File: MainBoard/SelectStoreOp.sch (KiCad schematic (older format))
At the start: 18 parts, among them U32 74ABT245, U33 74ABT245, U34 74AHCT138, U35 74ABT245, U36 74ABT245, U37 74ABT245, U38 74ABT245, U39 74ABT245, U40 74ABT245

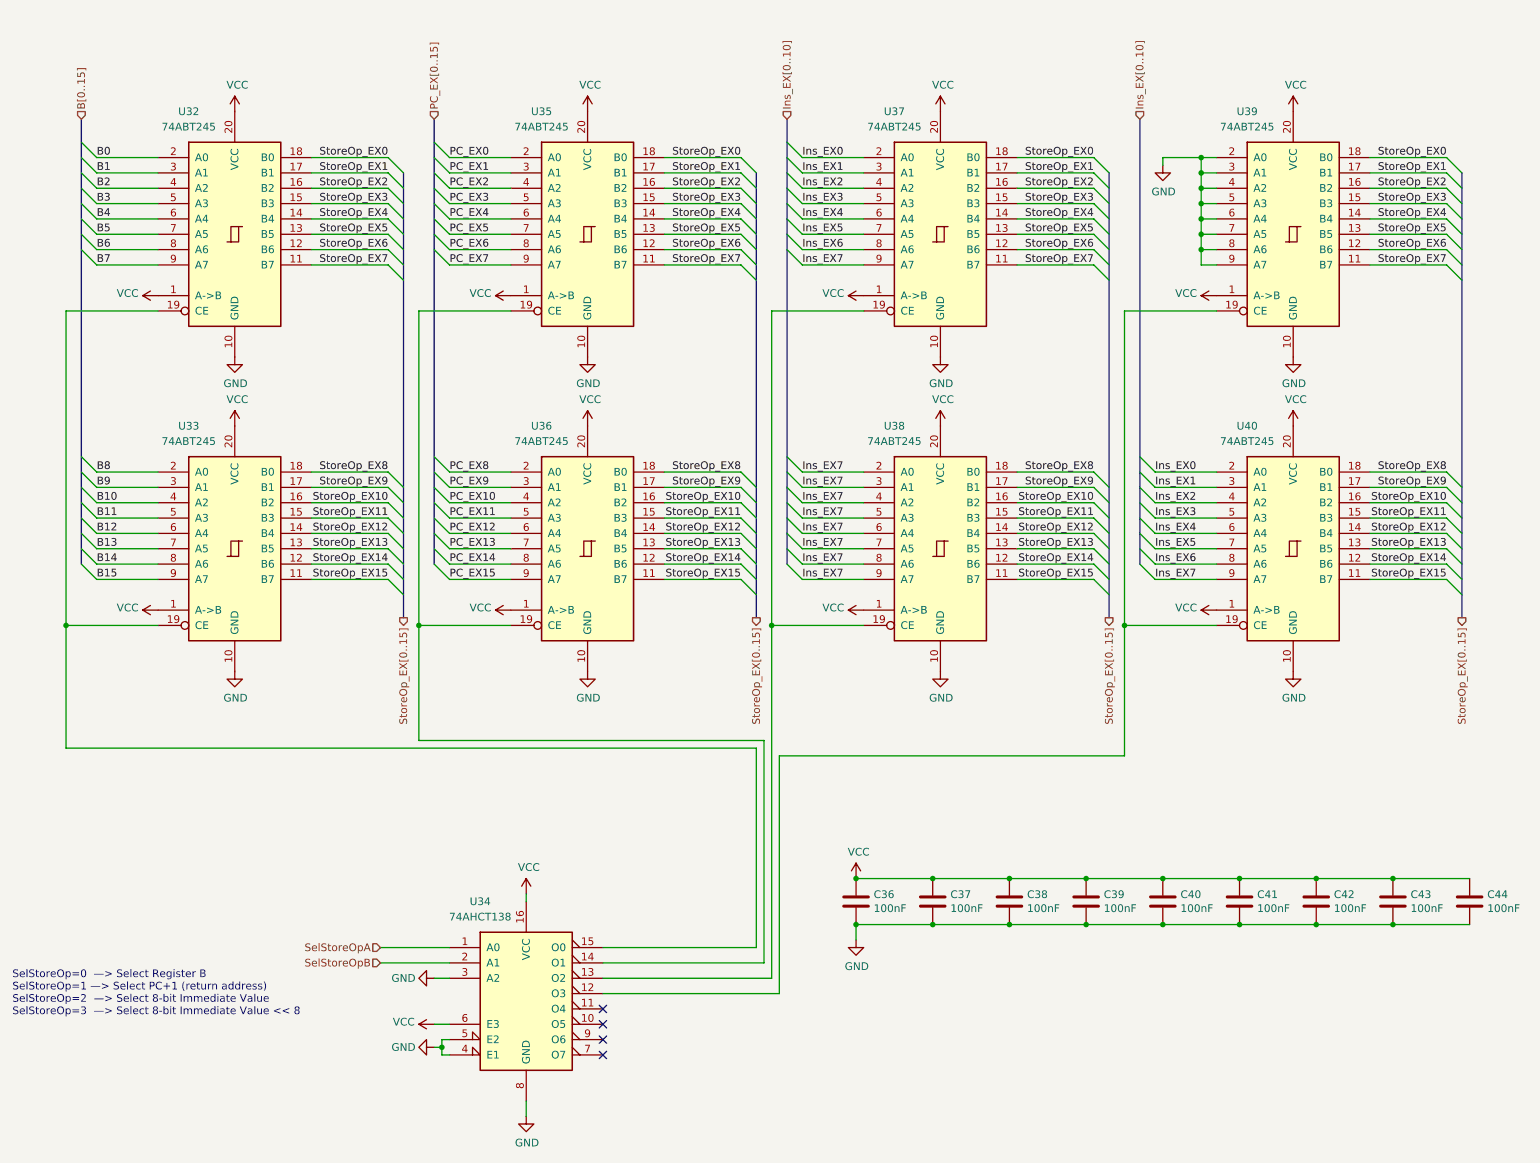
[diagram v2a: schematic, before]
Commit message: Replace 74AHCT245 with 74AHCT16245. Ditto 74ABT25.
This greatly reduces the number of components and saves a lot of board
space. (Note that PCB layout has been undone in areas related to changes.)
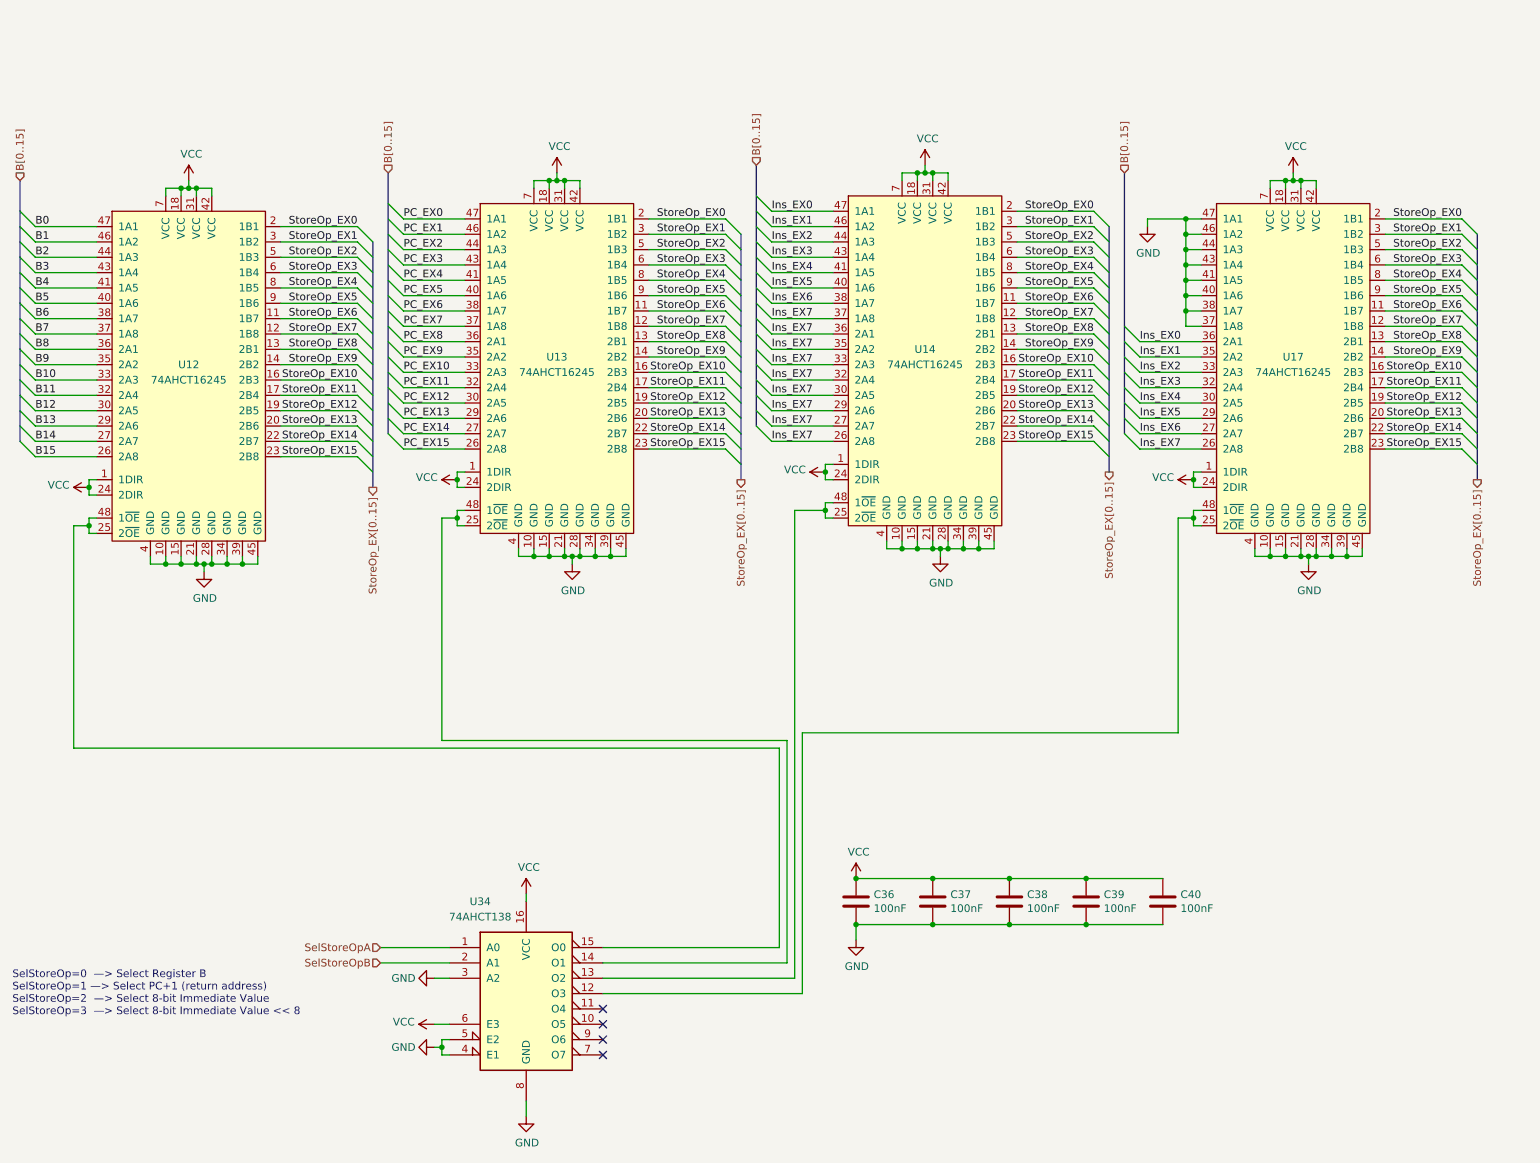
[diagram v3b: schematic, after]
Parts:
- removed C41, C42, C43, C44: 100nF, Capacitor_SMD:C_0603_1608Metric_Pad1.08x0.95mm_HandSolder, symbol Device:C
- removed U32, U33, U35, U36, U37, U38, U39, U40: 74ABT245, Package_SO:TSSOP-20_4.4x6.5mm_P0.65mm, symbol MainBoard-rescue:74LS245-74xx
- added U12, U13, U14, U17: 74AHCT16245, Package_SO:TSSOP-48_6.1x12.5mm_P0.5mm, symbol 74xx:74AHCT16245
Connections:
- net B0: now also U12.47 (1A1)
- net B1: now also U12.46 (1A2)
- net B10: now also U12.33 (2A3)
- net B11: now also U12.32 (2A4)
- net B12: now also U12.30 (2A5)
- net B13: now also U12.29 (2A6)
- net B14: now also U12.27 (2A7)
- net B15: now also U12.26 (2A8)
- net B2: now also U12.44 (1A3)
- net B3: now also U12.43 (1A4)
- net B4: now also U12.41 (1A5)
- net B5: now also U12.40 (1A6)
- net B6: now also U12.38 (1A7)
- net B7: now also U12.37 (1A8)
- net B8: now also U12.36 (2A1)
- net B9: now also U12.35 (2A2)
- net GND: now also U12.10 (GND), U12.15 (GND), U12.21 (GND), U12.28 (GND), U12.34 (GND), U12.39 (GND), U12.4 (GND), U12.45 (GND), U13.10 (GND), U13.15 (GND), U13.21 (GND), U13.28 (GND), U13.34 (GND), U13.39 (GND), U13.4 (GND), U13.45 (GND), U14.10 (GND), U14.15 (GND), U14.21 (GND), U14.28 (GND), U14.34 (GND), U14.39 (GND), U14.4 (GND), U14.45 (GND), U17.10 (GND), U17.15 (GND), U17.21 (GND), U17.28 (GND), U17.34 (GND), U17.37 (1A8), U17.38 (1A7), U17.39 (GND), U17.4 (GND), U17.40 (1A6), U17.41 (1A5), U17.43 (1A4), U17.44 (1A3), U17.45 (GND), U17.46 (1A2), U17.47 (1A1)
- net Ins_EX0: now also U14.47 (1A1), U17.36 (2A1)
- net Ins_EX1: now also U14.46 (1A2), U17.35 (2A2)
- net Ins_EX2: now also U14.44 (1A3), U17.33 (2A3)
- net Ins_EX3: now also U14.43 (1A4), U17.32 (2A4)
- net Ins_EX4: now also U14.41 (1A5), U17.30 (2A5)
- net Ins_EX5: now also U14.40 (1A6), U17.29 (2A6)
- net Ins_EX6: now also U14.38 (1A7), U17.27 (2A7)
- net Ins_EX7: now also U14.26 (2A8), U14.27 (2A7), U14.29 (2A6), U14.30 (2A5), U14.32 (2A4), U14.33 (2A3), U14.35 (2A2), U14.36 (2A1), U14.37 (1A8), U17.26 (2A8)
- net PC_EX0: now also U13.47 (1A1)
- net PC_EX1: now also U13.46 (1A2)
- net PC_EX10: now also U13.33 (2A3)
- net PC_EX11: now also U13.32 (2A4)
- net PC_EX12: now also U13.30 (2A5)
- net PC_EX13: now also U13.29 (2A6)
- net PC_EX14: now also U13.27 (2A7)
- net PC_EX15: now also U13.26 (2A8)
- net PC_EX2: now also U13.44 (1A3)
- net PC_EX3: now also U13.43 (1A4)
- net PC_EX4: now also U13.41 (1A5)
- net PC_EX5: now also U13.40 (1A6)
- net PC_EX6: now also U13.38 (1A7)
- net PC_EX7: now also U13.37 (1A8)
- net PC_EX8: now also U13.36 (2A1)
- net PC_EX9: now also U13.35 (2A2)
- net StoreOp_EX0: now also U12.2 (1B1), U13.2 (1B1), U14.2 (1B1), U17.2 (1B1)
- net StoreOp_EX1: now also U12.3 (1B2), U13.3 (1B2), U14.3 (1B2), U17.3 (1B2)
- net StoreOp_EX10: now also U12.16 (2B3), U13.16 (2B3), U14.16 (2B3), U17.16 (2B3)
- net StoreOp_EX11: now also U12.17 (2B4), U13.17 (2B4), U14.17 (2B4), U17.17 (2B4)
- net StoreOp_EX12: now also U12.19 (2B5), U13.19 (2B5), U14.19 (2B5), U17.19 (2B5)
- net StoreOp_EX13: now also U12.20 (2B6), U13.20 (2B6), U14.20 (2B6), U17.20 (2B6)
- net StoreOp_EX14: now also U12.22 (2B7), U13.22 (2B7), U14.22 (2B7), U17.22 (2B7)
- net StoreOp_EX15: now also U12.23 (2B8), U13.23 (2B8), U14.23 (2B8), U17.23 (2B8)
- net StoreOp_EX2: now also U12.5 (1B3), U13.5 (1B3), U14.5 (1B3), U17.5 (1B3)
- net StoreOp_EX3: now also U12.6 (1B4), U13.6 (1B4), U14.6 (1B4), U17.6 (1B4)
- net StoreOp_EX4: now also U12.8 (1B5), U13.8 (1B5), U14.8 (1B5), U17.8 (1B5)
- net StoreOp_EX5: now also U12.9 (1B6), U13.9 (1B6), U14.9 (1B6), U17.9 (1B6)
- net StoreOp_EX6: now also U12.11 (1B7), U13.11 (1B7), U14.11 (1B7), U17.11 (1B7)
- net StoreOp_EX7: now also U12.12 (1B8), U13.12 (1B8), U14.12 (1B8), U17.12 (1B8)
- net StoreOp_EX8: now also U12.13 (2B1), U13.13 (2B1), U14.13 (2B1), U17.13 (2B1)
- net StoreOp_EX9: now also U12.14 (2B2), U13.14 (2B2), U14.14 (2B2), U17.14 (2B2)
- net VCC: now also U12.1 (1DIR), U12.18 (VCC), U12.24 (2DIR), U12.31 (VCC), U12.42 (VCC), U12.7 (VCC), U13.1 (1DIR), U13.18 (VCC), U13.24 (2DIR), U13.31 (VCC), U13.42 (VCC), U13.7 (VCC), U14.1 (1DIR), U14.18 (VCC), U14.24 (2DIR), U14.31 (VCC), U14.42 (VCC), U14.7 (VCC), U17.1 (1DIR), U17.18 (VCC), U17.24 (2DIR), U17.31 (VCC), U17.42 (VCC), U17.7 (VCC)
- net at U34.12 (O3): now also U17.25 (2~OE), U17.48 (1~OE)
- net at U34.13 (O2): now also U14.25 (2~OE), U14.48 (1~OE)
- net at U34.14 (O1): now also U13.25 (2~OE), U13.48 (1~OE)
- net at U34.15 (O0): now also U12.25 (2~OE), U12.48 (1~OE)

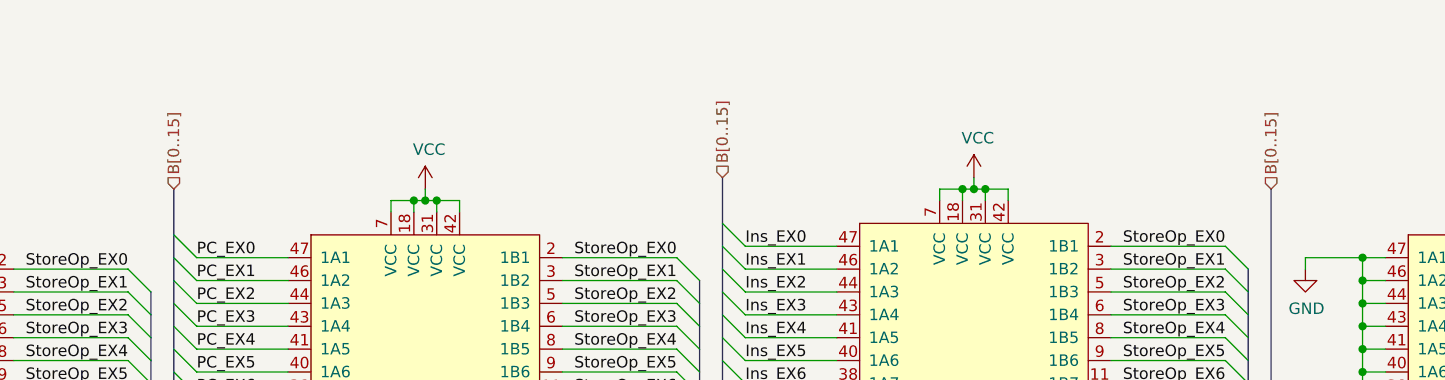
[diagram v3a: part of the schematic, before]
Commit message: Replace 74AHCT574 with 74ABT16374
This greatly reduces the number of components on the PCB and the amount
of board space needed for the CPU.
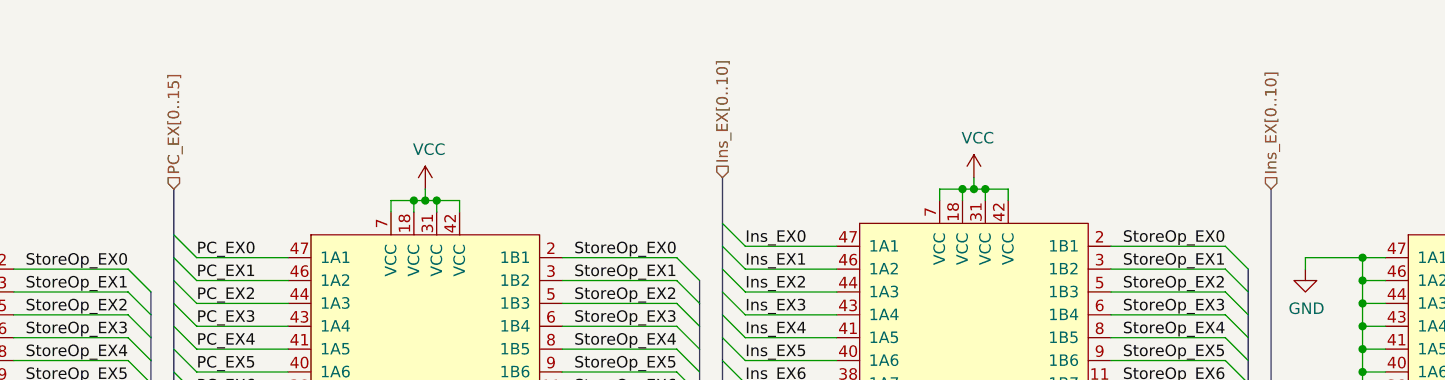
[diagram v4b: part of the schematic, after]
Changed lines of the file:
@@
 $EndComp
 Text HLabel 3100 1600 1    50   Input ~ 0
-B[0..15]
+PC_EX[0..15]
 Wire Wire Line
 	5300 2600 4800 2600
@@
 $EndComp
 Text HLabel 5500 1550 1    50   Input ~ 0
-B[0..15]
+Ins_EX[0..10]
 Wire Wire Line
 	7700 2550 7200 2550
@@
 $EndComp
 Text HLabel 7900 1600 1    50   Input ~ 0
-B[0..15]
+Ins_EX[0..10]
 Wire Wire Line
 	10100 2600 9600 2600
